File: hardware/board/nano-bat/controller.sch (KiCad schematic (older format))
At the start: 42 parts, among them J301 Conn_ARM_JTAG_SWD_10, J302 Conn_01x10, J303 Conn_01x10, SW301 SW_Push, SW302 SW_Push, SW303 SW_Push, SW304 SW_Push, U301 M95256-WMN6P, U302 STM32L452CEUx

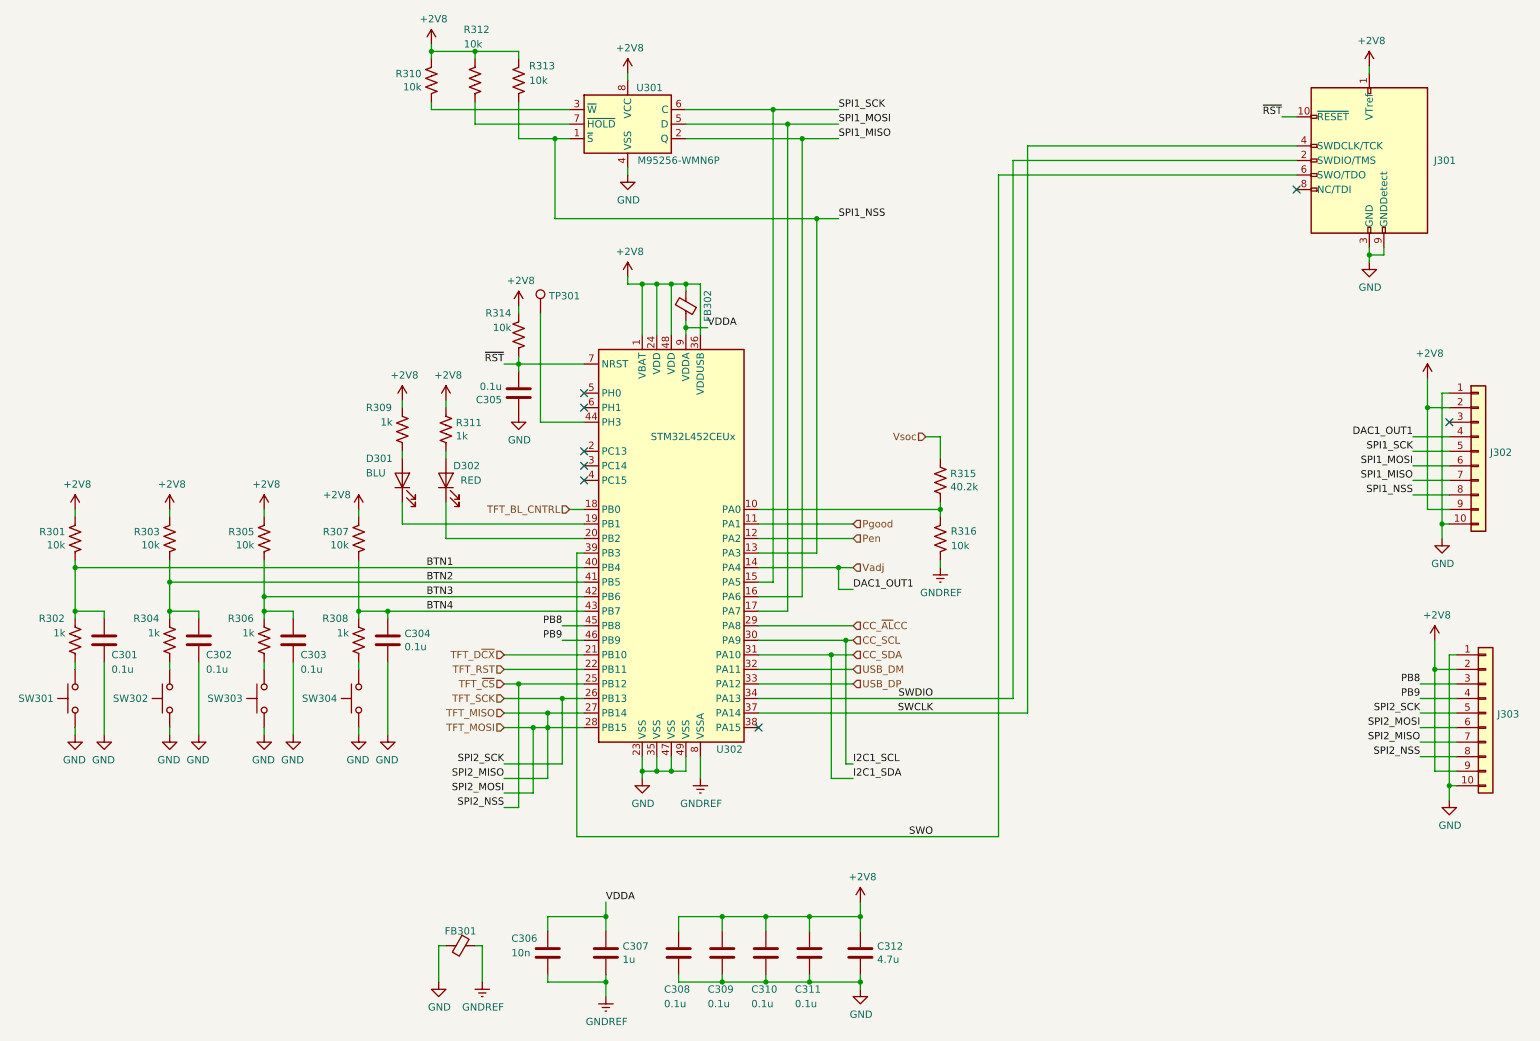
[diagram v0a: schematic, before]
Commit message: Adding test points, initial board outline
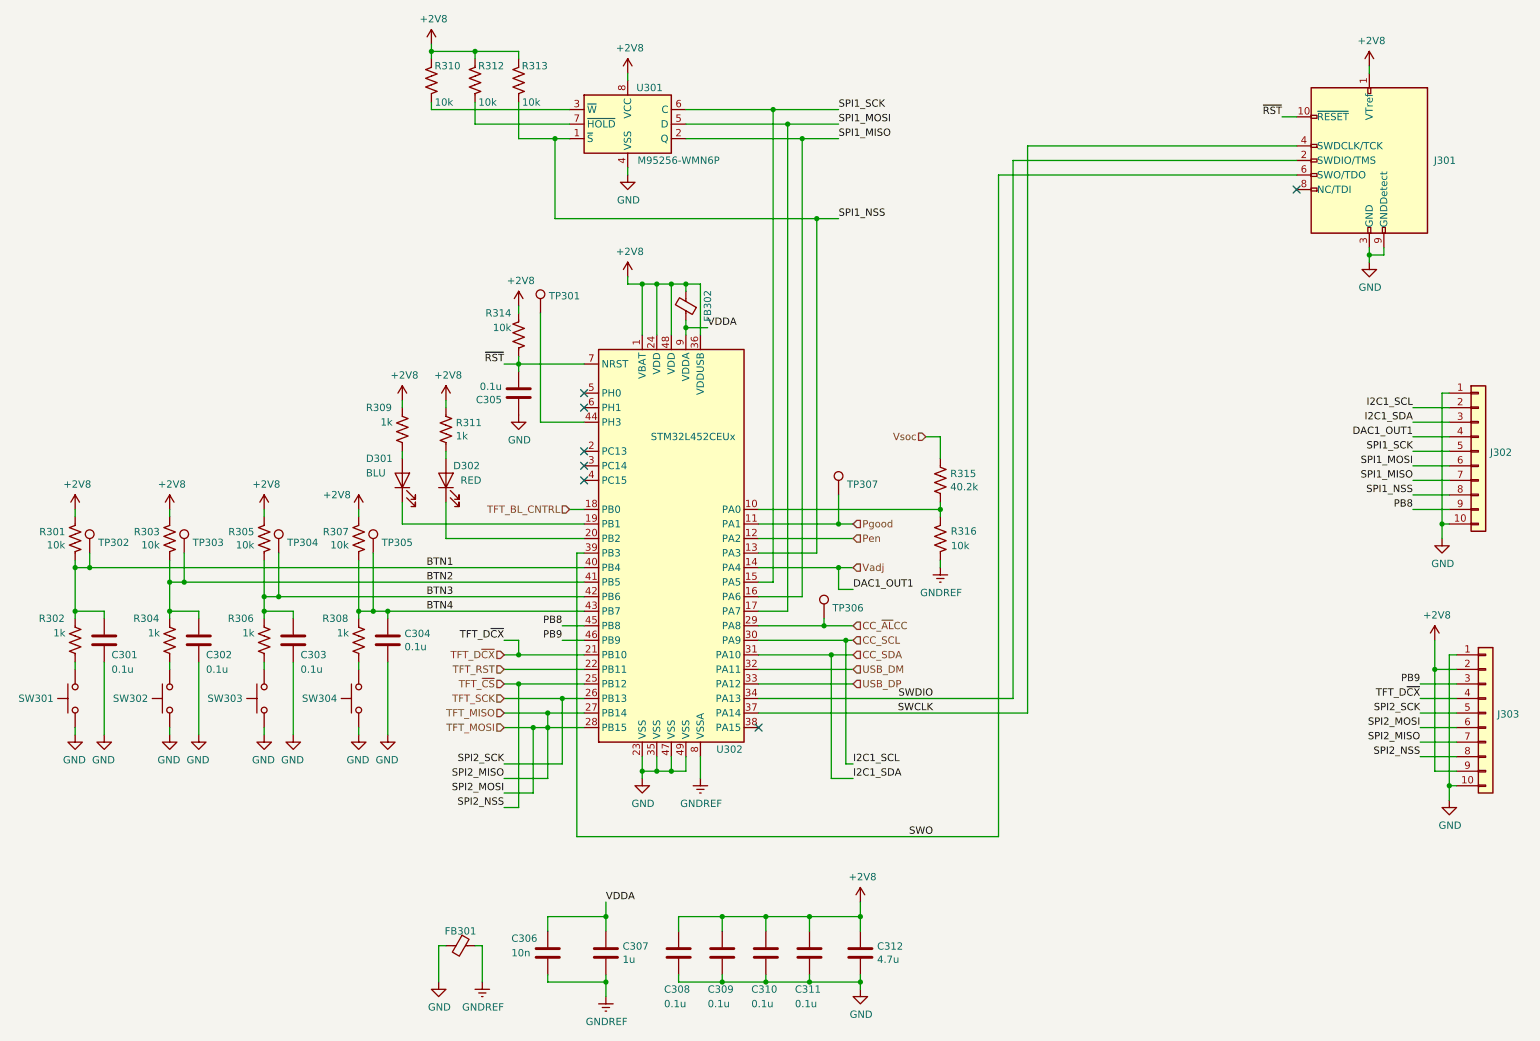
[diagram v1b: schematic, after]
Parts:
- added TP302, TP303, TP304, TP305, TP306, TP307: TestPoint, TestPoint:TestPoint_Pad_D1.0mm, symbol Connector:TestPoint
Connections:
- net +2V8: no longer J302.2 (Pin_2), J302.9 (Pin_9)
- net BTN1: now also TP302.1
- net BTN2: now also TP303.1
- net BTN3: now also TP304.1
- net BTN4: now also TP305.1
- net CC_SCL: now also J302.2 (Pin_2)
- net CC_SDA: now also J302.3 (Pin_3)
- net CC_~AL~CC: now also TP306.1
- net PB8: now also J302.9 (Pin_9); no longer J303.3 (Pin_3)
- net PB9: now also J303.3 (Pin_3); no longer J303.4 (Pin_4)
- net Pgood: now also TP307.1
- net TFT_D~CX: now also J303.4 (Pin_4)
- no-connect marks 8 -> 7
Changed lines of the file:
@@
 Text Label 10100 3950 2    50   ~ 0
 SPI1_NSS
-Connection ~ 10200 3350
-Wire Wire Line
-	10200 4050 10350 4050
-Wire Wire Line
-	10200 3350 10200 4050
-Wire Wire Line
-	10200 3350 10350 3350
-Wire Wire Line
-	10200 3150 10200 3350
 Connection ~ 10300 4150
 Wire Wire Line
@@
 	9800 2300 9800 2350
 NoConn ~ 9300 1850
-Text Label 10100 3550 2    50   ~ 0
-DAC1_OUT1
 Wire Wire Line
 	10100 3550 10350 3550
@@
 	4300 4050 4400 4050
 Wire Wire Line
-	6250 4150 5600 4150
+	6250 4150 6150 4150
 Wire Wire Line
 	4200 2050 6000 2050
@@
 Text Label 4250 4850 2    50   ~ 0
 PB8
-Text Label 10150 5250 2    50   ~ 0
+Text Label 10100 4050 2    50   ~ 0
 PB8
-Text Label 10150 5350 2    50   ~ 0
+Text Label 10150 5250 2    50   ~ 0
 PB9
 Wire Wire Line
@@
 	7450 1550 9300 1550
 $Comp
-L power:+2V8 #PWR0130
-U 1 1 5E4DE792
-P 10200 3150
-F 0 "#PWR0130" H 10200 3000 50  0001 C CNN
-F 1 "+2V8" H 10215 3323 50  0000 C CNN
-F 2 "" H 10200 3150 50  0001 C CNN
-F 3 "" H 10200 3150 50  0001 C CNN
-	1    10200 3150
-	1    0    0    -1
-$EndComp
-$Comp
 L power:+2V8 #PWR0131
 U 1 1 5E4DF04B
@@
 Connection ~ 2850 4750
 Wire Wire Line
-	3050 4750 2850 4750
+	3050 4750 2950 4750
 Wire Wire Line
 	900  4400 900  4450
@@
 	1550 4400 1550 4550
 Wire Wire Line
-	4400 4450 900  4450
+	4400 4450 1000 4450
 Connection ~ 900  4450
 Wire Wire Line
@@
 	1550 4550 1550 4750
 Wire Wire Line
-	4400 4650 2200 4650
+	4400 4650 2300 4650
 Connection ~ 2200 4650
 Wire Wire Line
@@
 	2200 4400 2200 4650
 Wire Wire Line
-	1550 4550 4400 4550
+	1550 4550 1650 4550
 Wire Wire Line
 	3050 4750 4400 4750
@@
 U 1 1 5E485978
 P 3350 1100
-F 0 "R310" H 3418 1146 50  0000 L CNN
-F 1 "10k" H 3418 1055 50  0000 L CNN
+F 0 "R310" H 3150 1200 50  0000 L CNN
+F 1 "10k" H 3200 950 50  0000 L CNN
 F 2 "Resistor_SMD:R_0603_1608Metric" V 3390 1090 50  0001 C CNN
 F 3 "~" H 3350 1100 50  0001 C CNN
@@
 $EndComp
 $Comp
-L Device:R_US R312
-U 1 1 5E494A9B
-P 3650 1100
-F 0 "R312" H 3550 1450 50  0000 L CNN
-F 1 "10k" H 3600 1350 50  0000 L CNN
-F 2 "Resistor_SMD:R_0603_1608Metric" V 3690 1090 50  0001 C CNN
-F 3 "~" H 3650 1100 50  0001 C CNN
-F 4 "311-10KGRCT-ND" H 3650 1100 50  0001 C CNN "Part"
-	1    3650 1100
-	-1   0    0    -1
-$EndComp
-$Comp
 L Device:R_US R313
 U 1 1 5E4A3BBE
 P 3950 1100
-F 0 "R313" H 3700 1200 50  0000 L CNN
-F 1 "10k" H 3750 1100 50  0000 L CNN
+F 0 "R313" H 3750 1200 50  0000 L CNN
+F 1 "10k" H 3800 950 50  0000 L CNN
 F 2 "Resistor_SMD:R_0603_1608Metric" V 3990 1090 50  0001 C CNN
 F 3 "~" H 3950 1100 50  0001 C CNN
@@
 	6850 4050 6850 4000
 Wire Wire Line
-	6250 4850 5600 4850
+	6250 4850 6050 4850
 $Comp
 L Device:R_US R316
@@
 	-1   0    0    -1
 $EndComp
-NoConn ~ 10350 3450
 $Comp
 L Connector:TestPoint TP301
@@
 	3850 5150 4400 5150
 Wire Wire Line
-	3850 5050 4400 5050
+	3850 5050 3950 5050
 Wire Wire Line
 	4150 5550 4150 5900
@@
 Wire Wire Line
 	4350 4350 4350 6300
+Text Label 10100 3550 2    50   ~ 0
+DAC1_OUT1
+Text Label 10100 3450 2    50   ~ 0
+I2C1_SDA
+Text Label 10100 3350 2    50   ~ 0
+I2C1_SCL
+Wire Wire Line
+	10100 3350 10350 3350
+Wire Wire Line
+	10350 3450 10100 3450
+$Comp
+L Device:R_US R312
+U 1 1 5E494A9B
+P 3650 1100
+F 0 "R312" H 3450 1200 50  0000 L CNN
+F 1 "10k" H 3500 950 50  0000 L CNN
+F 2 "Resistor_SMD:R_0603_1608Metric" V 3690 1090 50  0001 C CNN
+F 3 "~" H 3650 1100 50  0001 C CNN
+F 4 "311-10KGRCT-ND" H 3650 1100 50  0001 C CNN "Part"
+	1    3650 1100
+	-1   0    0    -1
+$EndComp
+$Comp
+L Connector:TestPoint TP302
+U 1 1 5E27D0B0
+P 1000 4350
+F 0 "TP302" H 1058 4422 50  0000 L CNN
+F 1 "TestPoint" H 1058 4377 50  0001 L CNN
+F 2 "TestPoint:TestPoint_Pad_D1.0mm" H 1200 4350 50  0001 C CNN
+F 3 "~" H 1200 4350 50  0001 C CNN
+	1    1000 4350
+	1    0    0    -1
+$EndComp
+$Comp
+L Connector:TestPoint TP303
+U 1 1 5E27D3EA
+P 1650 4350
+F 0 "TP303" H 1708 4422 50  0000 L CNN
+F 1 "TestPoint" H 1708 4377 50  0001 L CNN
+F 2 "TestPoint:TestPoint_Pad_D1.0mm" H 1850 4350 50  0001 C CNN
+F 3 "~" H 1850 4350 50  0001 C CNN
+	1    1650 4350
+	1    0    0    -1
+$EndComp
+$Comp
+L Connector:TestPoint TP304
+U 1 1 5E27D5E6
+P 2300 4350
+F 0 "TP304" H 2358 4422 50  0000 L CNN
+F 1 "TestPoint" H 2358 4377 50  0001 L CNN
+F 2 "TestPoint:TestPoint_Pad_D1.0mm" H 2500 4350 50  0001 C CNN
+F 3 "~" H 2500 4350 50  0001 C CNN
+	1    2300 4350
+	1    0    0    -1
+$EndComp
+$Comp
+L Connector:TestPoint TP305
+U 1 1 5E27D86D
+P 2950 4350
+F 0 "TP305" H 3008 4422 50  0000 L CNN
+F 1 "TestPoint" H 3008 4377 50  0001 L CNN
+F 2 "TestPoint:TestPoint_Pad_D1.0mm" H 3150 4350 50  0001 C CNN
+F 3 "~" H 3150 4350 50  0001 C CNN
+	1    2950 4350
+	1    0    0    -1
+$EndComp
+Wire Wire Line
+	2950 4350 2950 4750
+Connection ~ 2950 4750
+Wire Wire Line
+	2950 4750 2850 4750
+Wire Wire Line
+	2300 4350 2300 4650
+Connection ~ 2300 4650
+Wire Wire Line
+	2300 4650 2200 4650
+Wire Wire Line
+	1650 4350 1650 4550
+Connection ~ 1650 4550
+Wire Wire Line
+	1650 4550 4400 4550
+Wire Wire Line
+	1000 4350 1000 4450
+Connection ~ 1000 4450
+Wire Wire Line
+	1000 4450 900  4450
+Text Label 3850 4950 2    50   ~ 0
+TFT_D~CX
+Wire Wire Line
+	3850 4950 3950 4950
+Wire Wire Line
+	3950 4950 3950 5050
+Connection ~ 3950 5050
+Wire Wire Line
+	3950 5050 4400 5050
+Text Label 10150 5350 2    50   ~ 0
+TFT_D~CX
+Wire Wire Line
+	10100 4050 10350 4050
+$Comp
+L Connector:TestPoint TP306
+U 1 1 5E2F53FA
+P 6050 4800
+F 0 "TP306" H 6108 4872 50  0000 L CNN
+F 1 "TestPoint" H 6108 4827 50  0001 L CNN
+F 2 "TestPoint:TestPoint_Pad_D1.0mm" H 6250 4800 50  0001 C CNN
+F 3 "~" H 6250 4800 50  0001 C CNN
+	1    6050 4800
+	1    0    0    -1
+$EndComp
+Wire Wire Line
+	6050 4800 6050 4850
+Connection ~ 6050 4850
+Wire Wire Line
+	6050 4850 5600 4850
+$Comp
+L Connector:TestPoint TP307
+U 1 1 5E307AB0
+P 6150 3950
+F 0 "TP307" H 6208 4022 50  0000 L CNN
+F 1 "TestPoint" H 6208 3977 50  0001 L CNN
+F 2 "TestPoint:TestPoint_Pad_D1.0mm" H 6350 3950 50  0001 C CNN
+F 3 "~" H 6350 3950 50  0001 C CNN
+	1    6150 3950
+	1    0    0    -1
+$EndComp
+Wire Wire Line
+	6150 4150 6150 3950
+Connection ~ 6150 4150
+Wire Wire Line
+	6150 4150 5600 4150
 $EndSCHEMATC
